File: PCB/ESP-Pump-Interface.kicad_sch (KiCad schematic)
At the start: 24 parts, among them J1 USB_C_Receptacle_PowerOnly_6P, Q1 2N2219, Q2 2N2219, Q3 2N2219, Q4 2N2219, U1 DOIT-ESP32-DEVKIT-V1

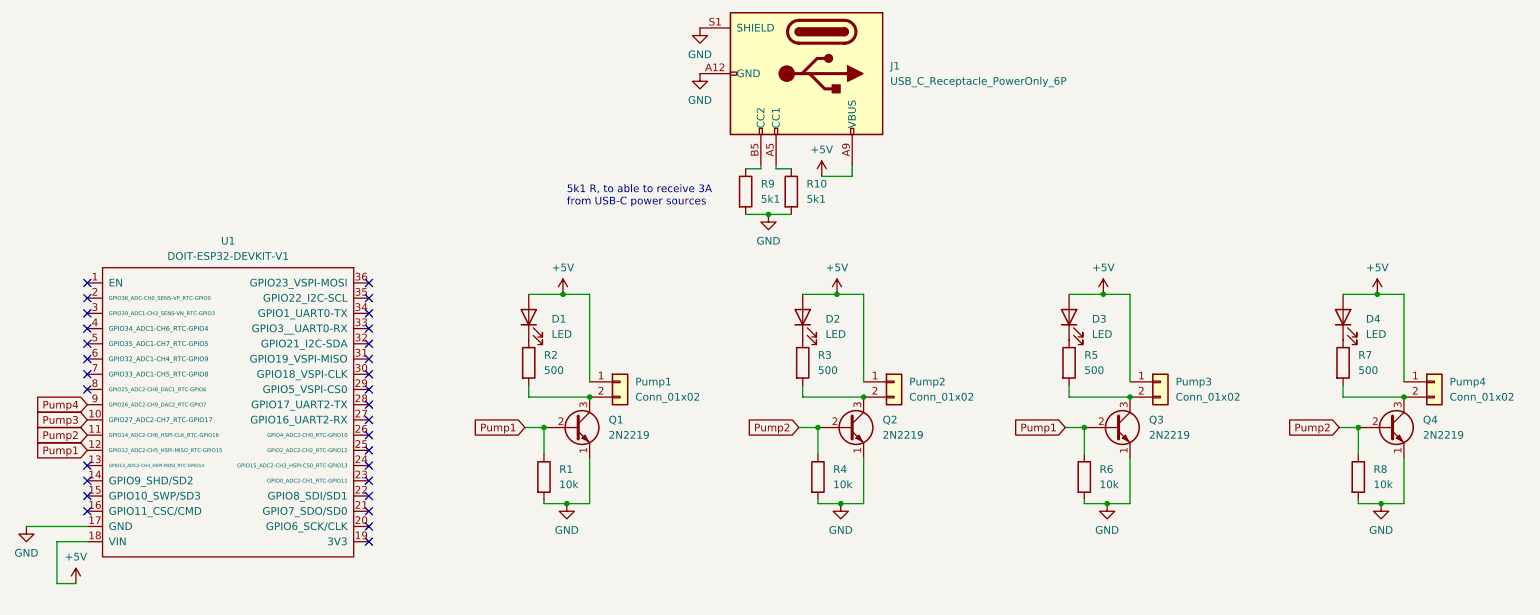
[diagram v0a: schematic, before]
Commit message: changed esp32-doit-devkit V1 symbol and footprint (source: SNAPEDA)
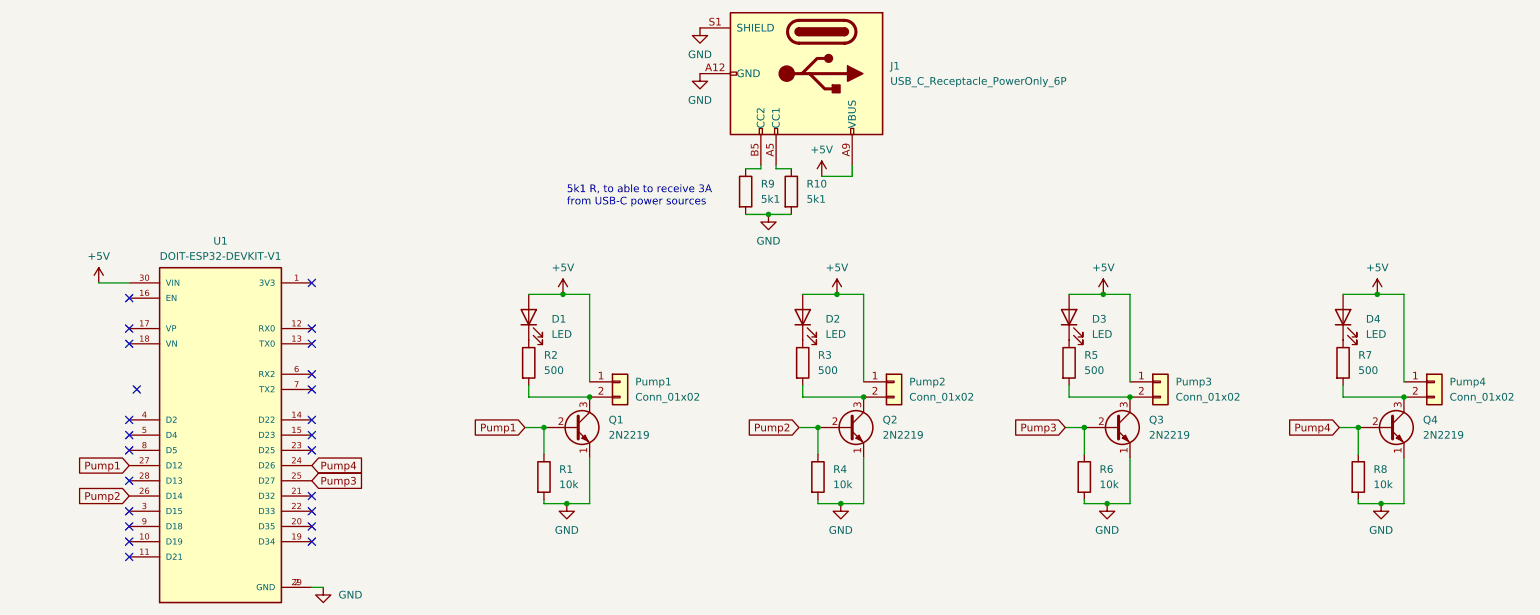
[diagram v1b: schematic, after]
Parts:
- U1: footprint doit-esp32-devkit-kicad-master:ESP32-DOIT-DEVKIT -> ESP32-DEVKIT-V1:MODULE_ESP32_DEVKIT_V1; symbol doit-esp32-devkit-v1:DOIT-ESP32-DEVKIT-V1 -> ESP32-DEVKIT-V1:ESP32-DEVKIT-V1; Availability (none) -> Not in stock; Check_prices (none) -> https://www.snapeda.com/parts/ESP32-DEVKIT-V1/Do+it/view-pa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; MANUFACTURER (none) -> DOIT; MAXIMUM_PACKAGE_HEIGHT (none) -> 6.8 mm; MF (none) -> Do it; MP (none) -> ESP32-DEVKIT-V1; PARTREV (none) -> N/A; Package (none) -> None; Price (none) -> None; STANDARD (none) -> Manufacturer Recommendations; SnapEDA_Link (none) -> https://www.snapeda.com/parts/ESP32-DEVKIT-V1/Do+it/view-pa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
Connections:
- net +5V: now also U1.30 (VIN); no longer U1.18 (VIN)
- net GND: now also U1.2 (GND), U1.29 (GND); no longer U1.17 (GND)
- net Pump1: now also U1.27 (D12); no longer Q3.2 (B), R6.1, U1.12 (GPIO12_ADC2-CH5_HSPI-MISO_RTC-GPIO15)
- net Pump2: now also U1.26 (D14); no longer Q4.2 (B), R8.1, U1.11 (GPIO14_ADC2-CH6_HSPI-CLK_RTC-GPIO16)
- net Pump3: now also Q3.2 (B), R6.1, U1.25 (D27); no longer U1.10 (GPIO27_ADC2-CH7_RTC-GPIO17)
- net Pump4: now also Q4.2 (B), R8.1, U1.24 (D26); no longer U1.9 (GPIO26_ADC2-CH9_DAC2_RTC-GPIO7)
- no-connect marks 30 -> 24
